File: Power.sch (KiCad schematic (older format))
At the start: 26 parts, among them U1 LP2985-3.3, U3 LP2985-3.3, U5 MP4561_QFN10

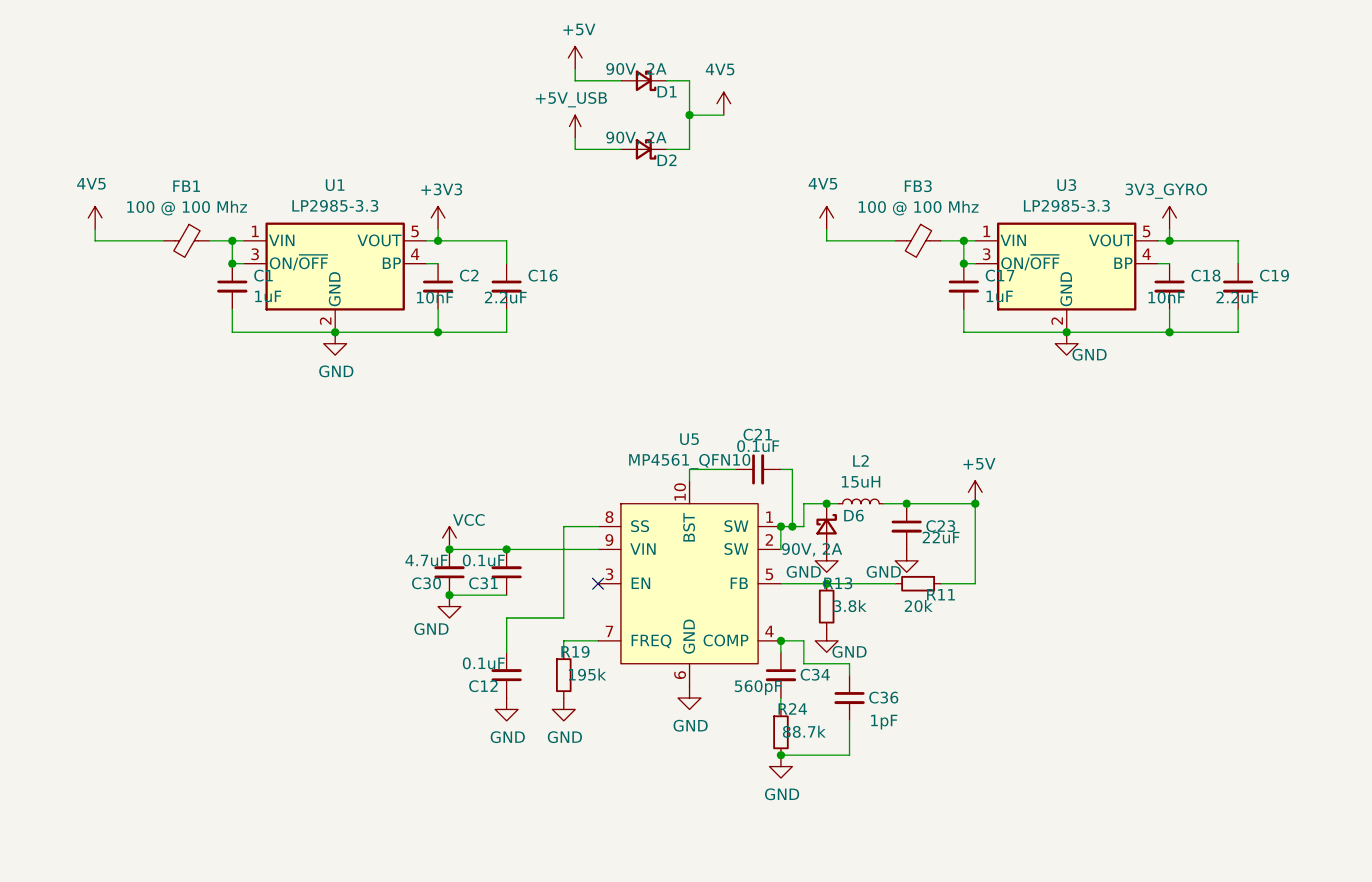
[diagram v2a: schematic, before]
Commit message: Changed some components to match what is in stock
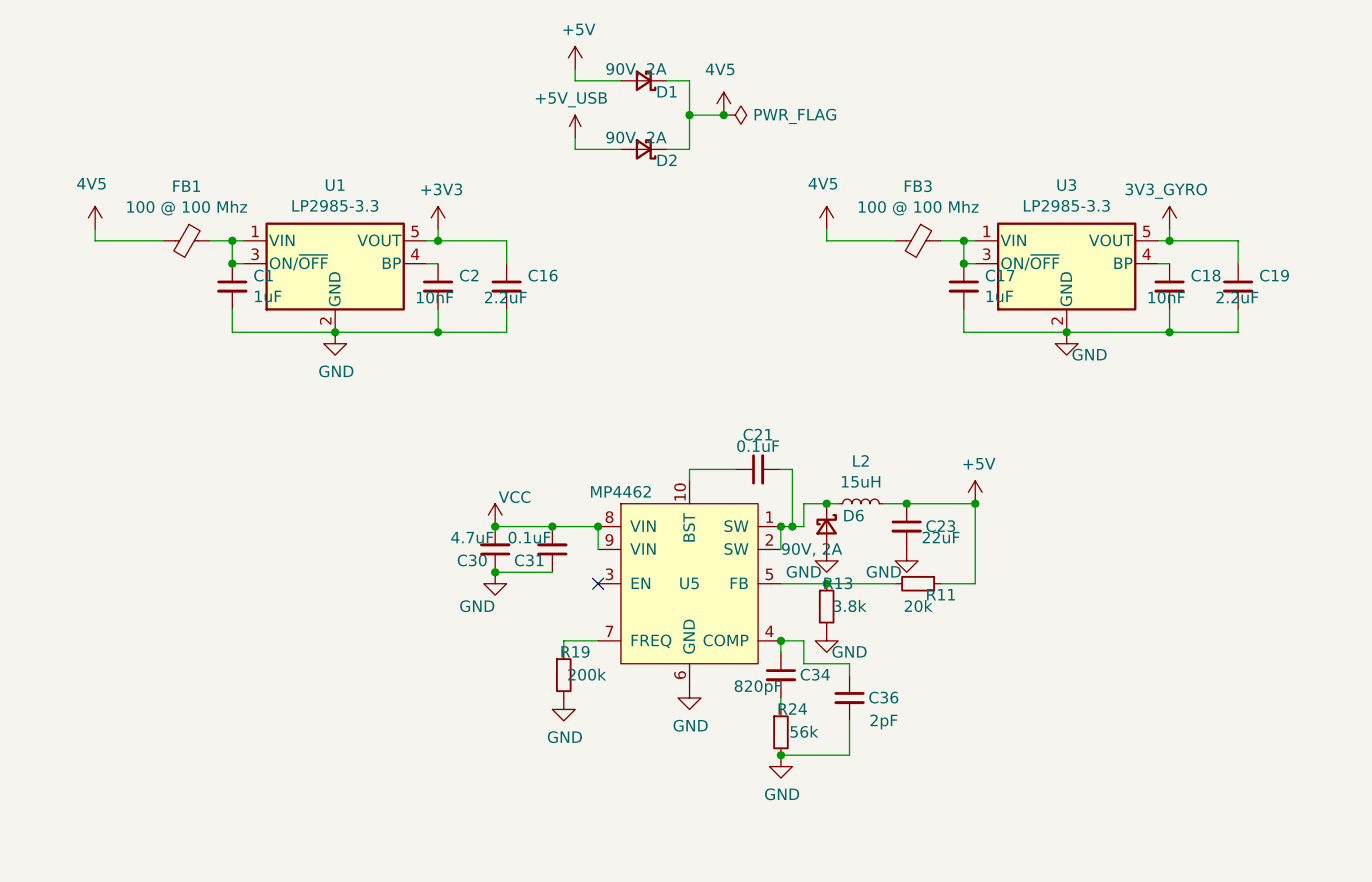
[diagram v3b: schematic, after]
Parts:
- removed C12: 0.1uF, Capacitor_SMD:C_0402_1005Metric, symbol Device:C_Small
- removed U5: MP4561_QFN10, Package_DFN_QFN:DFN-10-1EP_3x3mm_P0.5mm_EP1.7x2.5mm, symbol Regulator_Switching:MP4561_QFN10
- added U5: MP4462, Package_DFN_QFN:DFN-10-1EP_3x3mm_P0.5mm_EP1.7x2.5mm, symbol Regulator_Switching:MP4462
- C34: value 560pF -> 820pF
- C36: value 1pF -> 2pF
- L2: footprint Inductor_SMD:L_XGL4030 -> Inductor_SMD:L_Bourns-SRN3015
- R19: value 195k -> 200k
- R24: value 88.7k -> 56k
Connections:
- net GND: now also U5.6 (GND)
- net VCC: now also U5.8 (VIN), U5.9 (VIN)
- net at C34.1, C36.1: now also U5.4 (COMP)
- net at R11.2, R13.1: now also U5.5 (FB)
- net at C21.2, D6.1 (K), L2.1: now also U5.1 (SW), U5.2 (SW)
- net at R19.1: now also U5.7 (FREQ)
- net at C21.1: now also U5.10 (BST)
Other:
- moved on the sheet: C30, C31
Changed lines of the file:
@@
 	6000 5100 6000 5150
 Wire Wire Line
-	4550 4450 4800 4450
-Connection ~ 4550 4450
-Wire Wire Line
-	4550 4650 4800 4650
-Connection ~ 4550 4650
+	4750 4350 5000 4350
+Connection ~ 4750 4350
+Wire Wire Line
+	4750 4550 5000 4550
+Connection ~ 4750 4550
 $Comp
 L Device:C_Small C?
 U 1 1 60967A9B
-P 4800 4550
+P 5000 4450
 AR Path="/60967A9B" Ref="C?"  Part="1"
 AR Path="/6094AC2B/60967A9B" Ref="C31"  Part="1"
-F 0 "C31" H 4900 4600 50  0000 C CNN
-F 1 "0.1uF" H 4900 4500 50  0000 C CNN
-F 2 "Capacitor_SMD:C_0402_1005Metric" H 4800 4550 50  0001 C CNN
-F 3 "~" H 4800 4550 50  0001 C CNN
-	1    4800 4550
+F 0 "C31" H 5100 4500 50  0000 C CNN
+F 1 "0.1uF" H 5100 4400 50  0000 C CNN
+F 2 "Capacitor_SMD:C_0402_1005Metric" H 5000 4450 50  0001 C CNN
+F 3 "~" H 5000 4450 50  0001 C CNN
+	1    5000 4450
 	-1   0    0    1
 $EndComp
@@
 L Device:C_Small C?
 U 1 1 60967AA1
-P 4550 4550
+P 4750 4450
 AR Path="/60967AA1" Ref="C?"  Part="1"
 AR Path="/6094AC2B/60967AA1" Ref="C30"  Part="1"
-F 0 "C30" H 4650 4600 50  0000 C CNN
-F 1 "4.7uF" H 4650 4500 50  0000 C CNN
-F 2 "Capacitor_SMD:C_0603_1608Metric" H 4550 4550 50  0001 C CNN
-F 3 "~" H 4550 4550 50  0001 C CNN
-	1    4550 4550
+F 0 "C30" H 4850 4500 50  0000 C CNN
+F 1 "4.7uF" H 4850 4400 50  0000 C CNN
+F 2 "Capacitor_SMD:C_0603_1608Metric" H 4750 4450 50  0001 C CNN
+F 3 "~" H 4750 4450 50  0001 C CNN
+	1    4750 4450
 	-1   0    0    1
 $EndComp
@@
 AR Path="/6094AC2B/60967AAE" Ref="C36"  Part="1"
 F 0 "C36" H 6450 5100 50  0000 C CNN
-F 1 "1pF" H 6450 5000 50  0000 C CNN
+F 1 "2pF" H 6450 5000 50  0000 C CNN
 F 2 "Capacitor_SMD:C_0402_1005Metric" H 6300 5100 50  0001 C CNN
 F 3 "~" H 6300 5100 50  0001 C CNN
@@
 AR Path="/6094AC2B/60967ACC" Ref="R24"  Part="1"
 F 0 "R24" H 6050 5350 50  0000 C CNN
-F 1 "88.7k" H 6100 5250 50  0000 C CNN
+F 1 "56k" H 6100 5250 50  0000 C CNN
 F 2 "Resistor_SMD:R_0402_1005Metric" H 6000 5250 50  0001 C CNN
 F 3 "~" H 6000 5250 50  0001 C CNN
@@
 AR Path="/6094AC2B/60967AD2" Ref="C34"  Part="1"
 F 0 "C34" H 6150 5000 50  0000 C CNN
-F 1 "560pF" H 5900 4950 50  0000 C CNN
+F 1 "820pF" H 5900 4950 50  0000 C CNN
 F 2 "Capacitor_SMD:C_0402_1005Metric" H 6000 5000 50  0001 C CNN
 F 3 "~" H 6000 5000 50  0001 C CNN
@@
 F 0 "L2" V 6535 4250 50  0000 C CNN
 F 1 "15uH" V 6444 4250 50  0000 C CNN
-F 2 "Inductor_SMD:L_XGL4030" H 6350 4250 50  0001 C CNN
+F 2 "Inductor_SMD:L_Bourns-SRN3015" H 6350 4250 50  0001 C CNN
 F 3 "~" H 6350 4250 50  0001 C CNN
 	1    6350 4250
@@
 AR Path="/6094AC2B/60967B1F" Ref="R19"  Part="1"
 F 0 "R19" H 5100 5100 50  0000 C CNN
-F 1 "195k" H 5150 5000 50  0000 C CNN
+F 1 "200k" H 5150 5000 50  0000 C CNN
 F 2 "Resistor_SMD:R_0402_1005Metric" H 5050 5000 50  0001 C CNN
 F 3 "~" H 5050 5000 50  0001 C CNN
@@
 L power:GND #PWR?
 U 1 1 60967B25
-P 4550 4650
+P 4750 4550
 AR Path="/60967B25" Ref="#PWR?"  Part="1"
 AR Path="/6094AC2B/60967B25" Ref="#PWR0119"  Part="1"
-F 0 "#PWR0119" H 4550 4400 50  0001 C CNN
-F 1 "GND" H 4550 4500 50  0000 R CNN
-F 2 "" H 4550 4650 50  0001 C CNN
-F 3 "" H 4550 4650 50  0001 C CNN
-	1    4550 4650
+F 0 "#PWR0119" H 4750 4300 50  0001 C CNN
+F 1 "GND" H 4750 4400 50  0000 R CNN
+F 2 "" H 4750 4550 50  0001 C CNN
+F 3 "" H 4750 4550 50  0001 C CNN
+	1    4750 4550
 	1    0    0    -1
 $EndComp
@@
 L power:VCC #PWR?
 U 1 1 60967B37
-P 4550 4450
+P 4750 4350
 AR Path="/60967B37" Ref="#PWR?"  Part="1"
 AR Path="/6094AC2B/60967B37" Ref="#PWR0120"  Part="1"
-F 0 "#PWR0120" H 4550 4300 50  0001 C CNN
-F 1 "VCC" H 4565 4577 50  0000 L CNN
-F 2 "" H 4550 4450 50  0001 C CNN
-F 3 "" H 4550 4450 50  0001 C CNN
-	1    4550 4450
+F 0 "#PWR0120" H 4750 4200 50  0001 C CNN
+F 1 "VCC" H 4765 4477 50  0000 L CNN
+F 2 "" H 4750 4350 50  0001 C CNN
+F 3 "" H 4750 4350 50  0001 C CNN
+	1    4750 4350
 	1    0    0    -1
 $EndComp
@@
 	1    0    0    -1
 $EndComp
-Wire Wire Line
-	4800 4450 5200 4450
-Connection ~ 4800 4450
-$Comp
-L Device:C_Small C?
-U 1 1 60D96081
-P 4800 5000
-AR Path="/60D96081" Ref="C?"  Part="1"
-AR Path="/6094AC2B/60D96081" Ref="C12"  Part="1"
-F 0 "C12" H 4900 5050 50  0000 C CNN
-F 1 "0.1uF" H 4900 4950 50  0000 C CNN
-F 2 "Capacitor_SMD:C_0402_1005Metric" H 4800 5000 50  0001 C CNN
-F 3 "~" H 4800 5000 50  0001 C CNN
-	1    4800 5000
-	-1   0    0    1
-$EndComp
-Wire Wire Line
-	5050 4350 5200 4350
-$Comp
-L power:GND #PWR?
-U 1 1 60D991B3
-P 4800 5100
-AR Path="/60D991B3" Ref="#PWR?"  Part="1"
-AR Path="/6094AC2B/60D991B3" Ref="#PWR0105"  Part="1"
-F 0 "#PWR0105" H 4800 4850 50  0001 C CNN
-F 1 "GND" H 4805 4927 50  0000 C CNN
-F 2 "" H 4800 5100 50  0001 C CNN
-F 3 "" H 4800 5100 50  0001 C CNN
-	1    4800 5100
-	1    0    0    -1
-$EndComp
-Wire Wire Line
-	5050 4750 4800 4750
-Wire Wire Line
-	4800 4750 4800 4900
-Wire Wire Line
-	5050 4350 5050 4750
-$Comp
-L Regulator_Switching:MP4561_QFN10 U5
-U 1 1 60DB77BA
+$Comp
+L power:PWR_FLAG #FLG0104
+U 1 1 60DB82B0
+P 5750 2550
+F 0 "#FLG0104" H 5750 2625 50  0001 C CNN
+F 1 "PWR_FLAG" V 5750 2678 50  0000 L CNN
+F 2 "" H 5750 2550 50  0001 C CNN
+F 3 "~" H 5750 2550 50  0001 C CNN
+	1    5750 2550
+	0    1    1    0
+$EndComp
+Connection ~ 5750 2550
+$Comp
+L Regulator_Switching:MP4462 U5
+U 1 1 60D9B1ED
 P 5600 4600
-F 0 "U5" H 5600 5231 50  0000 C CNN
-F 1 "MP4561_QFN10" H 5600 5140 50  0000 C CNN
-F 2 "Package_DFN_QFN:DFN-10-1EP_3x3mm_P0.5mm_EP1.7x2.5mm" H 5600 4600 50  0001 C CNN
-F 3 "" H 5600 4600 50  0001 C CNN
+F 0 "U5" H 5600 4600 50  0000 C CNN
+F 1 "MP4462" H 5300 5000 50  0000 C CNN
+F 2 "Package_DFN_QFN:DFN-10-1EP_3x3mm_P0.5mm_EP1.7x2.5mm" H 5600 5100 50  0001 C CNN
+F 3 "" H 5600 5100 50  0001 C CNN
 	1    5600 4600
 	1    0    0    -1
@@
 Connection ~ 6000 4350
 Connection ~ 6000 4850
+Wire Wire Line
+	5200 4450 5200 4350
+Wire Wire Line
+	5000 4350 5200 4350
+Connection ~ 5000 4350
+Connection ~ 5200 4350
 $EndSCHEMATC
